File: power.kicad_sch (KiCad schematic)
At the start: 14 parts, among them IC1 TPS63070RNMR

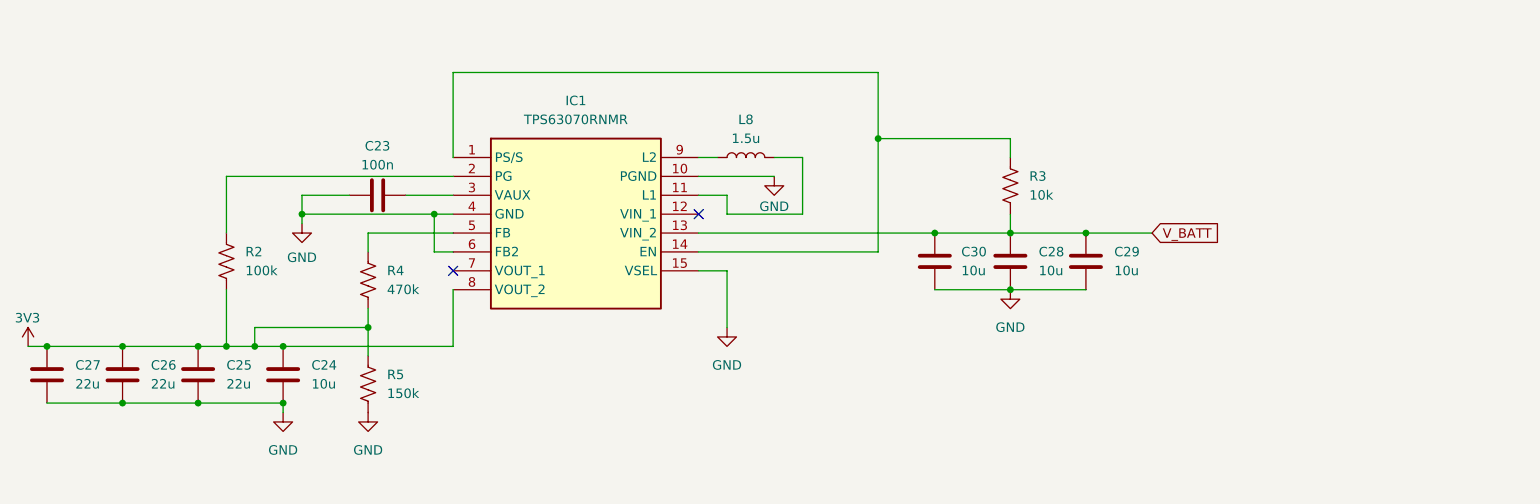
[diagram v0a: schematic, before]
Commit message: Add power supply voltage cutoff, start fixing radio schematic
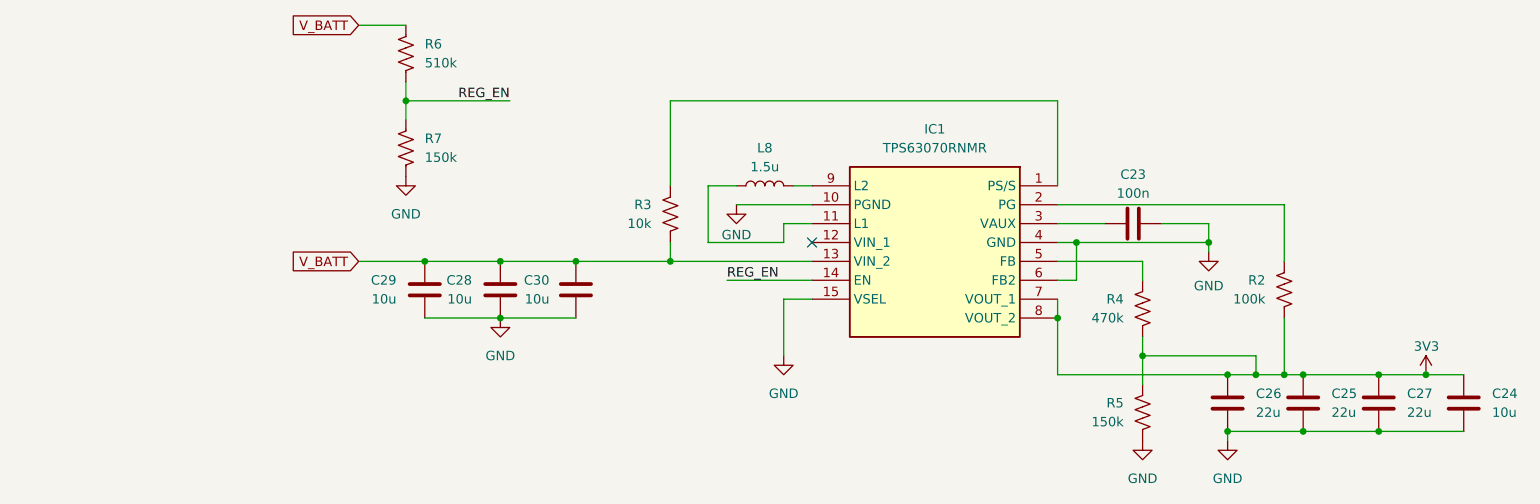
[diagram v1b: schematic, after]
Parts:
- added R6: 510k, symbol Device:R_US
- added R7: 150k, symbol Device:R_US
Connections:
- net 3V3: now also IC1.7 (VOUT_1)
- net GND: now also R7.2
- net V_BATT: now also R6.1
- net at IC1.1 (PS/S), R3.1: no longer IC1.14 (EN)
- new net REG_EN: IC1.14 (EN), R6.2, R7.1
- no-connect marks 2 -> 1
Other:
- moved on the sheet: C23, C24, C25, C26, C28, C29, C30, IC1, L8, R2, R3, R4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

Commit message: proper formating
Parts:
- removed R6: 510k, symbol Device:R_US
- removed R7: 150k, symbol Device:R_US
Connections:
- net REG_EN is gone; now on an unnamed net: IC1.14 (EN)
- net 3V3: no longer IC1.7 (VOUT_1)
- no-connect marks 1 -> 2
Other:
- moved on the sheet: C23, C24, C25, C26, C28, C29, C30, IC1, L8, R2, R3, R4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
